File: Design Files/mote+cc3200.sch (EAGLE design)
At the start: 13 parts, among them IC1 TPS6306X, U1 CC3200

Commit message: Updated Design Files and Libraries
Some libraries included in the design were added.
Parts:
- removed JP1: (no value), adafruit:PINHD-1X6CB
- added C5: 10 uF, eagle-ltspice:CC1808
- added C6: 0.1 uF, rcl:C-EUC1808
- added C7: 0.22 uF, capacitor-wima:C5/3.5
- added C8, C9: 0.1uF, capacitor-wima:C5/3.5
- added CN1: JTAG, adafruit:1X4-BIG
- added CN2: FLASH, adafruit:1X4-BIG
- added R10, R11, R4, R5, R6, R7, R8, R9: 2.2K, adafruit:R-US_0207/9
- added R12: 100K, resistor:R-US_0207/10
- added U2: WIND, WINDc:WIND
- added U3: SEN0219, SEN0219c:SEN0219
- added U4: LM393, LM393c:LM393
- added U5: LTP5902, LTP5902c:LTP5902
- added X1: HIH8121-021-001, con-JST PH:B4B-PH-K-S
- added X2: OPT3001, con-JST PH:B4B-PH-K-S
- added X3: ADXL362, con-JST PH:B4B-PH-K-S
- added X4: SEN0322, con-JST PH:B4B-PH-K-S
- C2: value 66 uF -> 56 uF; device eagle-ltspice:CC1808 -> rcl:CPOL-EUE3.5-8
- C3: value 20 uF -> 10 uF
- C4: value 0.1 uF -> 10 uF
- R1, R2: device eagle-ltspice:RR2010 -> rcl:R-EU_R5025
- R3: device eagle-ltspice:RR2010 -> rcl:R-EU_R1206
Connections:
- new net 3.3V: U5.GND, U5.GND1, U5.GND2, U5.GND3
- new net AO_0S: U1.GPIO0, U2.TMP
- new net AO_1S: U1.GPIO1, U2.RV
- new net AO_2S: U1.GPIO2, U3.SIG
- new net AO_3S: U1.GPIO3, U4.SIG
- new net DO_0: U5.GPIO17
- new net DO_1: U5.GPIO18
- new net FLASH_P_ENN: U5.FLASH_P_ENN
- new net FLS_SPI_CLK: CN2.1, U1.FLASH_SPI_CLK
- new net FLS_SPI_CS: CN2.4, U1.FLASH_SPI_CS
- new net FLS_SPI_DIN: CN2.3, U1.FLASH_SPI_DIN
- new net FLS_SPI_DOUT: CN2.2, U1.FLASH_SPI_DOUT
- new net IPCS_MISO: U5.IPCS_MISO
- new net IPCS_MOSI: U5.IPCS_MOSI
- new net IPCS_SCK: U5.IPCS_SCK
- new net IPCS_SSN: U5.IPCS_SSN
- new net N$1: CN1.4, R12.2, U1.TCK
- new net N$2: CN1.3, U1.TMS
- new net N$3: CN1.2, U1.TDI
- new net N$4: CN1.1, U1.TDO
- net +3.3V: now also C7.1, C8.2, C9.1, R10.1, R11.1, R4.1, R5.1, R6.1, R7.1, U5.VSUPPLY, X1.1, X2.1, X3.1
- net +3.6V: now also C4.1, C5.1; no longer C3.1
- net +5V: now also C2.+, C3.1, R8.1, R9.1, U2.VCC, U3.VCC, U4.VCC, X4.1; no longer C2.1
- net GND: now also C2.-, C5.2, C6.2, C7.2, C8.1, C9.2, R12.1, U2.GND, U3.GND, U4.GND, U5.GND4, U5.GND5, U5.GND6, U5.GND7, U5.GND8, X1.4, X2.4, X3.4, X4.4; no longer C2.2
- net SCL: now also R10.2, R4.2, R6.2, R8.2, X1.2, X2.2, X3.2, X4.2
- net SDA: now also R11.2, R5.2, R7.2, R9.2, X1.3, X2.3, X3.3, X4.3
- net VAUX_TPS: now also C6.1; no longer C4.1
- net WK_UP: now also U5.GPIO19
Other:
- note added: "1.4"
- note added: "Preliminary schematic of a mote and the CC3200 microcontroller."
- note added: "Sensors."
- note removed: "1.0"
- note removed: "ADXL362"
- note removed: "AI_0"
- note removed: "AI_1"
- note removed: "AI_2"
- note removed: "AI_3"
- note removed: "FLASH_P_ENn"
- note removed: "GND"
- note removed: "GPIO17"
- note removed: "GPIO18"
- note removed: "GPIO19"
- note removed: "HIH8000"
- note removed: "IPCS_MISO"
- note removed: "IPCS_MOSI"
- note removed: "IPCS_SCK"
- note removed: "IPCS_SSn"
- note removed: "LM393"
- note removed: "OPT3001"
- note removed: "Preliminary schematic of a mote."
- note removed: "SEN0219"
- note removed: "SEN0322"
- note removed: "U2"
- note removed: "UARTC0_RX"
- note removed: "UARTC0_TX"
- note removed: "VCC"
- note removed: "VSUPPLY"
- note removed: "Wind Rev. C"

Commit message: Updated design files.
Overwritten original mote+cc3200 files to revision 1.5. Added CAM data files in zip folder for PCB fabrication.
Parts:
- removed CN2: FLASH, adafruit:1X4-BIG
- removed R11: 2.2K, adafruit:R-US_0207/9
- removed R12: 100K, resistor:R-US_0207/10
- removed R2: 1 M, rcl:R-EU_R5025
- removed U1: CC3200, CC3200:CC3200R1M2RGCR
- removed X4: SEN0322, con-JST PH:B4B-PH-K-S
- added AC1: ADXL345, ADXL345:ADXL345
- added C10, C11: 10 pF, eagle-ltspice:CC1808
- added C12, C16, C17, C19, C20, C22: 0.1 uF, rcl:C-EUC1808
- added C13: 0.1uF, capacitor-wima:C5/3.5
- added C14: 2.2 uF, eagle-ltspice:CC1808
- added C15: 0.22 uF, capacitor-wima:C5/3.5
- added C18, C21: 10 uF, eagle-ltspice:CC1808
- added D1: SP1002-01JTG, SamacSys_Parts:SP1002-01JTG
- added HDR1: 87831-1020, SamacSys_Parts:87831-1020
- added IC2: W25Q80DLSNIG_TR, SamacSys_Parts:W25Q80DLSNIG_TR
- added JP1, JP2, JP3: (no value), eagle-ltspice:RR0201
- added L2, L3: 2.2 uH, rcl:L-EUL3216C
- added LED1: 156120RS75000, SamacSys_Parts:156120RS75000
- added PB1: FSMSM, SamacSys_Parts:FSMSM
- added Q1, Q2, Q3, Q4: FQU20N06LTU, SamacSys_Parts:FQU20N06LTU
- added Q5: DMN2004WK-7, SamacSys_Parts:DMN2004WK-7
- added S1: EG1224, SamacSys_Parts:EG1224
- added U6: LM393, LM393c:LM393
- added Y1: 32.768 KHz, crystal-geyer_V1_0:KX-13
- BATT_2: value BATTERY_BR1225/FA -> 12BH23P-GR; device 52101-101-REV-A_v16:BATTERY_BR1225/FA -> SamacSys_Parts:12BH23P-GR
- C1: value 10 pF -> 10 uF
- C2: value 56 uF -> 10 uF; device rcl:CPOL-EUE3.5-8 -> eagle-ltspice:CC1808
- C3: value 10 uF -> 0.1uF; device eagle-ltspice:CC1808 -> capacitor-wima:C5/3.5
- C4, C5: value 10 uF -> 0.1 uF; device eagle-ltspice:CC1808 -> rcl:C-EUC1808
- C7: value 0.22 uF -> 10 pF; device capacitor-wima:C5/3.5 -> eagle-ltspice:CC1808
- C8: value 0.1uF -> 56 uF; device capacitor-wima:C5/3.5 -> rcl:CPOL-EUE3.5-8
- C9: value 0.1uF -> 10 uF; device capacitor-wima:C5/3.5 -> eagle-ltspice:CC1808
- R1: value 1 M -> 100K; device rcl:R-EU_R5025 -> resistor:R-US_0207/10
- R10: value 2.2K -> 270; device adafruit:R-US_0207/9 -> Resistor_Capacitor:WSLP1206R0500FEA
- R3: value 111 K -> 1 M; device rcl:R-EU_R1206 -> rcl:R-EU_R5025
- R4: value 2.2K -> 111 K; device adafruit:R-US_0207/9 -> rcl:R-EU_R1206
- R5: value 2.2K -> 1 M; device adafruit:R-US_0207/9 -> rcl:R-EU_R5025
- R6, R7, R8: value 2.2K -> 100 K; device adafruit:R-US_0207/9 -> rcl:R-EU_R1206
- R9: value 2.2K -> 10 K; device adafruit:R-US_0207/9 -> Resistor_Capacitor:WSLP1206R0500FEA
- U2: value WIND -> Value; device WINDc:WIND -> CC3200:CC3200R1M2RGCR
- U3: value SEN0219 -> LTP5902; device SEN0219c:SEN0219 -> LTP5902c:LTP5902
- U4: value LM393 -> WIND; device LM393c:LM393 -> WINDc:WIND
- U5: value LTP5902 -> SEN0219; device LTP5902c:LTP5902 -> SEN0219c:SEN0219
- X3: value ADXL362 -> SEN0322
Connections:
- removed net 3.3V: U5.GND, U5.GND1, U5.GND2, U5.GND3
- removed net AO_0S: U1.GPIO0, U2.TMP
- removed net AO_1S: U1.GPIO1, U2.RV
- removed net AO_2S: U1.GPIO2, U3.SIG
- removed net AO_3S: U1.GPIO3, U4.SIG
- removed net DO_0: U5.GPIO17
- removed net DO_1: U5.GPIO18
- removed net N$1: CN1.4, R12.2, U1.TCK
- removed net N$2: CN1.3, U1.TMS
- removed net N$3: CN1.2, U1.TDI
- removed net N$4: CN1.1, U1.TDO
- removed net WK_UP: IC1.EN, U1.GPIO11, U5.GPIO19
- new net DC_ANA2: JP2.1, U2.DCDC_ANA2_SW_N
- new net DC_DIGSW: L3.2, U2.DCDC_DIG_SW
- new net GPIO12: Q4.G, U2.GPIO12
- new net GPIO13: Q1.G, U2.GPIO13
- new net GPIO14: Q2.G, U2.GPIO14
- new net GPIO15: Q3.G, U2.GPIO15
- new net GPIO2: U2.GPIO2, U4.TMP
- new net GPIO22: IC1.EN, U2.GPIO22
- new net GPIO3: U2.GPIO3, U4.RV
- new net GPIO31: JP2.2
- new net GPIO4: U2.GPIO4, U5.SIG
- new net GPIO5: U2.GPIO5, U6.SIG
- new net JTCK: JP1.2, U2.SOP2
- new net L2_ANA: L2.2, U2.DCDC_ANA_SW
- new net LED1: LED1.A, R10.2
- new net Q1+: AC1.GND_1, AC1.GND_2, AC1.GND_3, C15.2, Q1.D, U6.GND, X1.4, X2.4
- new net Q2+: Q2.D, U4.GND
- new net Q3+: Q3.D, U5.GND
- new net Q4+: Q4.D, X3.4
- new net RESETN: HDR1.6, Q5.D, U3.RESETN
- new net RST_BTN: C13.2, PB1.1, Q5.G, R9.2
- new net TCK: CN1.4, JP1.1, R1.2, U2.TCK
- new net TDI: CN1.2, U2.TDI
- new net TDO: CN1.1, U2.TDO
- new net TMS: CN1.3, U2.TMS
- new net UARTC0_RX: HDR1.10, U2.GPIO17, U3.UARTC0_RX
- new net UARTC0_TX: HDR1.9, U2.GPIO16, U3.UARTC0_TX
- new net VCC_DCDC: JP3.2
- new net VDD_ANA1: C19.1, C20.1, C21.1, C22.1, L2.1, U2.LDO_IN1, U2.LDO_IN2, U2.VDD_ANA1
- new net VDD_ANA2: JP3.1, U2.VDD_ANA2
- new net VDD_DIG: C16.1, C17.1, C18.1, L3.1, U2.VDD_DIG1, U2.VDD_DIG2
- new net VDD_PULL: C5.1, U2.VDD_PLL
- new net VDD_RAM: C4.1, U2.VDD_RAM
- new net VSUPPLY: HDR1.7
- new net XTAL1: C11.1, U2.RTC_XTAL_P, Y1.2
- new net XTAL2: C10.1, U2.RTC_XTAL_N, Y1.1
- net +3.3V: now also AC1.VDD_I/O, C12.1, C14.1, C15.1, C3.1, D1.1, IC2.!HOLD_(IO3), IC2.!WP_(IO2), IC2.VCC, PB1.2, R8.2, S1.NO, U2.VIN_DCDC_ANA, U2.VIN_DCDC_DIG, U2.VIN_IO1, U2.VIN_IO2, U3.VSUPPLY, U6.VCC; no longer C7.1, C8.2, C9.1, R11.1, R4.1, R5.1, R6.1, R7.1, U1.VIN_DCDC_ANA, U1.VIN_DCDC_DIG, U1.VIN_DCDC_PA, U1.VIN_IO1, U1.VIN_IO2, U5.VSUPPLY, X3.1
- net +3.6V: now also BATT_2.2, C1.1, C2.1; no longer BATT_2.+, C4.1, C5.1
- net +5V: now also C8.+, C9.1, R3.2, R5.2, U5.VCC, X3.1; no longer C2.+, C3.1, R1.2, R2.2, R8.1, R9.1, U2.VCC, U3.VCC, X4.1
- net FB_TPS: now also C7.1, R4.2, R5.1; no longer C1.1, R2.1, R3.2
- net FLASH_P_ENN: now also HDR1.2, U3.FLASH_P_ENN; no longer U5.FLASH_P_ENN
- net FLS_SPI_CLK: now also IC2.CLK, R6.1, U2.FLASH_SPI_CLK; no longer CN2.1, U1.FLASH_SPI_CLK
- net FLS_SPI_CS: now also IC2.!CS, R8.1, U2.FLASH_SPI_CS; no longer CN2.4, U1.FLASH_SPI_CS
- net FLS_SPI_DIN: now also IC2.DO_(IO1), U2.FLASH_SPI_DIN; no longer CN2.3, U1.FLASH_SPI_DIN
- net FLS_SPI_DOUT: now also IC2.DI_(IO0), R7.1, U2.FLASH_SPI_DOUT; no longer CN2.2, U1.FLASH_SPI_DOUT
- net GND: now also BATT_2.1, C10.2, C11.2, C12.2, C13.1, C14.2, C16.2, C17.2, C18.2, C19.2, C2.2, C20.2, C21.2, C22.2, C8.-, D1.2, HDR1.8, IC2.GND, LED1.K, Q1.S, Q2.S, Q3.S, Q4.S, Q5.S, R1.1, R4.1, R6.2, R7.2, R9.1, S1.COM, U2.GND_TAB, U2.V0, U2.V1, U2.V10, U2.V11, U2.V12, U2.V13, U2.V14, U2.V15, U2.V16, U2.V17, U2.V18, U2.V19, U2.V2, U2.V20, U2.V21, U2.V22, U2.V23, U2.V24, U2.V25, U2.V26, U2.V27, U2.V28, U2.V29, U2.V3, U2.V30, U2.V31, U2.V32, U2.V33, U2.V34, U2.V35, U2.V36, U2.V37, U2.V38, U2.V39, U2.V4, U2.V40, U2.V41, U2.V42, U2.V43, U2.V44, U2.V45, U2.V46, U2.V47, U2.V48, U2.V5, U2.V6, U2.V7, U2.V8, U2.V9, U3.GND1, U3.GND2, U3.GND3, U3.GND4, U3.GND5, U3.GND6, U3.GND7, U3.GND8, U3.GND9, U3.SPIS_SCK/SCL; no longer BATT_2.-, C2.-, C8.1, R12.1, R3.1, U1.GND_TAB, U2.GND, U3.GND, U4.GND, U5.GND4, U5.GND5, U5.GND6, U5.GND7, U5.GND8, X1.4, X2.4, X3.4, X4.4
- net IPCS_MISO: now also HDR1.5, U3.IPCS_MISO; no longer U5.IPCS_MISO
- net IPCS_MOSI: now also U3.IPCS_MOSI; no longer U5.IPCS_MOSI
- net IPCS_SCK: now also HDR1.3; no longer U5.IPCS_SCK
- net IPCS_SSN: now also HDR1.1, U3.IPCS_SSN; no longer U5.IPCS_SSN
- net PG_TPS: now also R3.1; no longer R1.1
- net SCL: now also AC1.SCL/SCLK, U2.GPIO10; no longer R10.2, R4.2, R6.2, R8.2, U1.GPIO12, X4.2
- net SDA: now also AC1.SDA/SDI/SDIO, U2.GPIO11; no longer R11.2, R5.2, R7.2, R9.2, U1.GPIO13, X4.3
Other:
- note added: "1.5"
- note added: "CC3200 Via Nets"
- note added: "Schematic of a mote and the CC3200 microcontroller."
- note removed: "1"
- note removed: "1.4"
- note removed: "10"
- note removed: "11"
- note removed: "20"
- note removed: "30"
- note removed: "31"
- note removed: "32"
- note removed: "33"
- note removed: "34"
- note removed: "35"
- note removed: "36"
- note removed: "37"
- note removed: "39"
- note removed: "4"
- note removed: "42"
- note removed: "5"
- note removed: "51"
- note removed: "55"
- note removed: "56"
- note removed: "6"
- note removed: "66"
- note removed: "7"
- note removed: "8"
- note removed: "9"
- note removed: "Preliminary schematic of a mote and the CC3200 microcontroller."

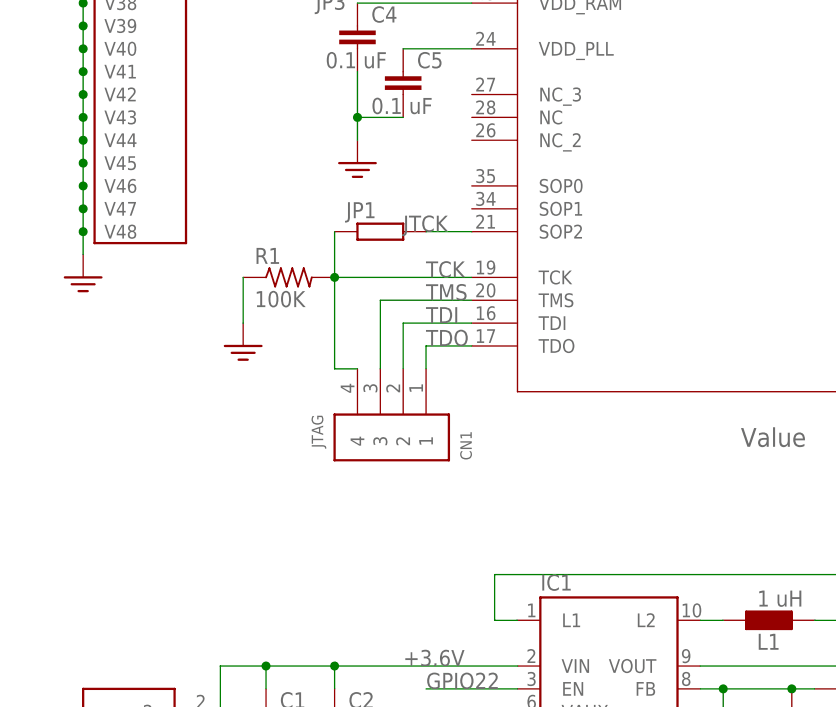
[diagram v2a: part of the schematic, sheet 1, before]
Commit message: Design files revised.
Added SOP connections to the design.
Ground stitched vias on the board were placed.
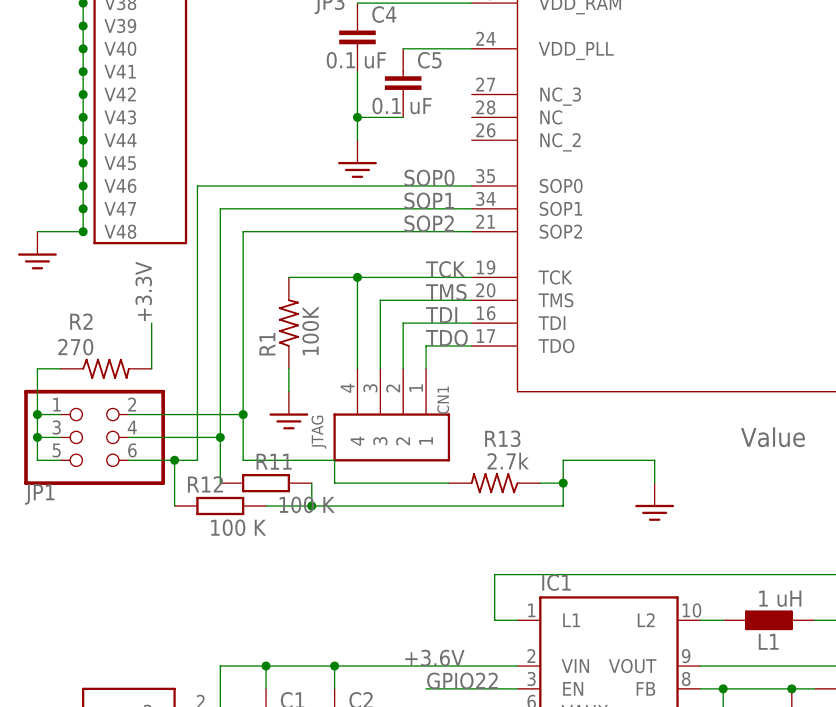
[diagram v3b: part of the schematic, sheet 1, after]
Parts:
- added R11, R12: 100 K, rcl:R-EU_R1206
- added R13: 2.7k, Resistor_Capacitor:WSLP1206R0500FEA
- added R2: 270, Resistor_Capacitor:WSLP1206R0500FEA
- JP1: device eagle-ltspice:RR0201 -> pinhead:PINHD-2X3/90
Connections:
- removed net JTCK: JP1.2, U2.SOP2
- new net JP1_PWR: JP1.1, JP1.3, JP1.5, R2.1
- new net SOP0: JP1.6, R12.1, U2.SOP0
- new net SOP1: JP1.4, R11.1, U2.SOP1
- new net SOP2: JP1.2, R13.2, U2.SOP2
- net +3.3V: now also R2.2
- net GND: now also R11.2, R12.2, R13.1
- net TCK: no longer JP1.1
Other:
- moved on the sheet: R1
